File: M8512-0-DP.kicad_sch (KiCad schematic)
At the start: 0 parts

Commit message: Starting DP03
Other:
- added sheet DP03 (DP03.kicad_sch)
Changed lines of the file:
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@@
+    )
+  )
+  (sheet (at 36.195 102.235) (size 21.59 16.51) (fields_autoplaced)
+    (stroke (width 0.1524) (type solid) (color 0 0 0 0))
+    (fill (color 0 0 0 0.0000))
+    (property "Sheet name" "DP03" (id 0) (at 36.195 101.5234 0)
+      (effects (font (size 1.27 1.27)) (justify left bottom))
+    )
+    (property "Sheet file" "DP03.kicad_sch" (id 1) (at 36.195 119.3296 0)
+      (effects (font (size 1.27 1.27)) (justify left top))
     )
   )
@@
     (path "/0d0df2ac-f3f7-482e-ba7c-5f666b048a62" (page "2"))
     (path "/e53a1afb-1269-4ccc-9d39-72635457c7f7" (page "3"))
+    (path "/37ba04c2-b201-4f29-919c-bcd861d42582" (page "4"))
   )
   (symbol_instances
+    (path "/37ba04c2-b201-4f29-919c-bcd861d42582/3263b06a-f347-437b-94aa-a857004a7ea1"
+      (reference "E4") (unit 1) (value "MC10181") (footprint "")
+    )
+    (path "/37ba04c2-b201-4f29-919c-bcd861d42582/938d047d-ccaa-40b8-b822-1670ea770fee"
+      (reference "E7") (unit 1) (value "MC10109") (footprint "")
+    )
+    (path "/37ba04c2-b201-4f29-919c-bcd861d42582/d079f1e9-2d2b-44e5-ae40-de8d878751b0"
+      (reference "E7") (unit 2) (value "MC10109") (footprint "")
+    )
     (path "/0d0df2ac-f3f7-482e-ba7c-5f666b048a62/0f39e560-9336-4a48-a641-fec45e29a92d"
       (reference "E?") (unit 1) (value "MC10141") (footprint "")

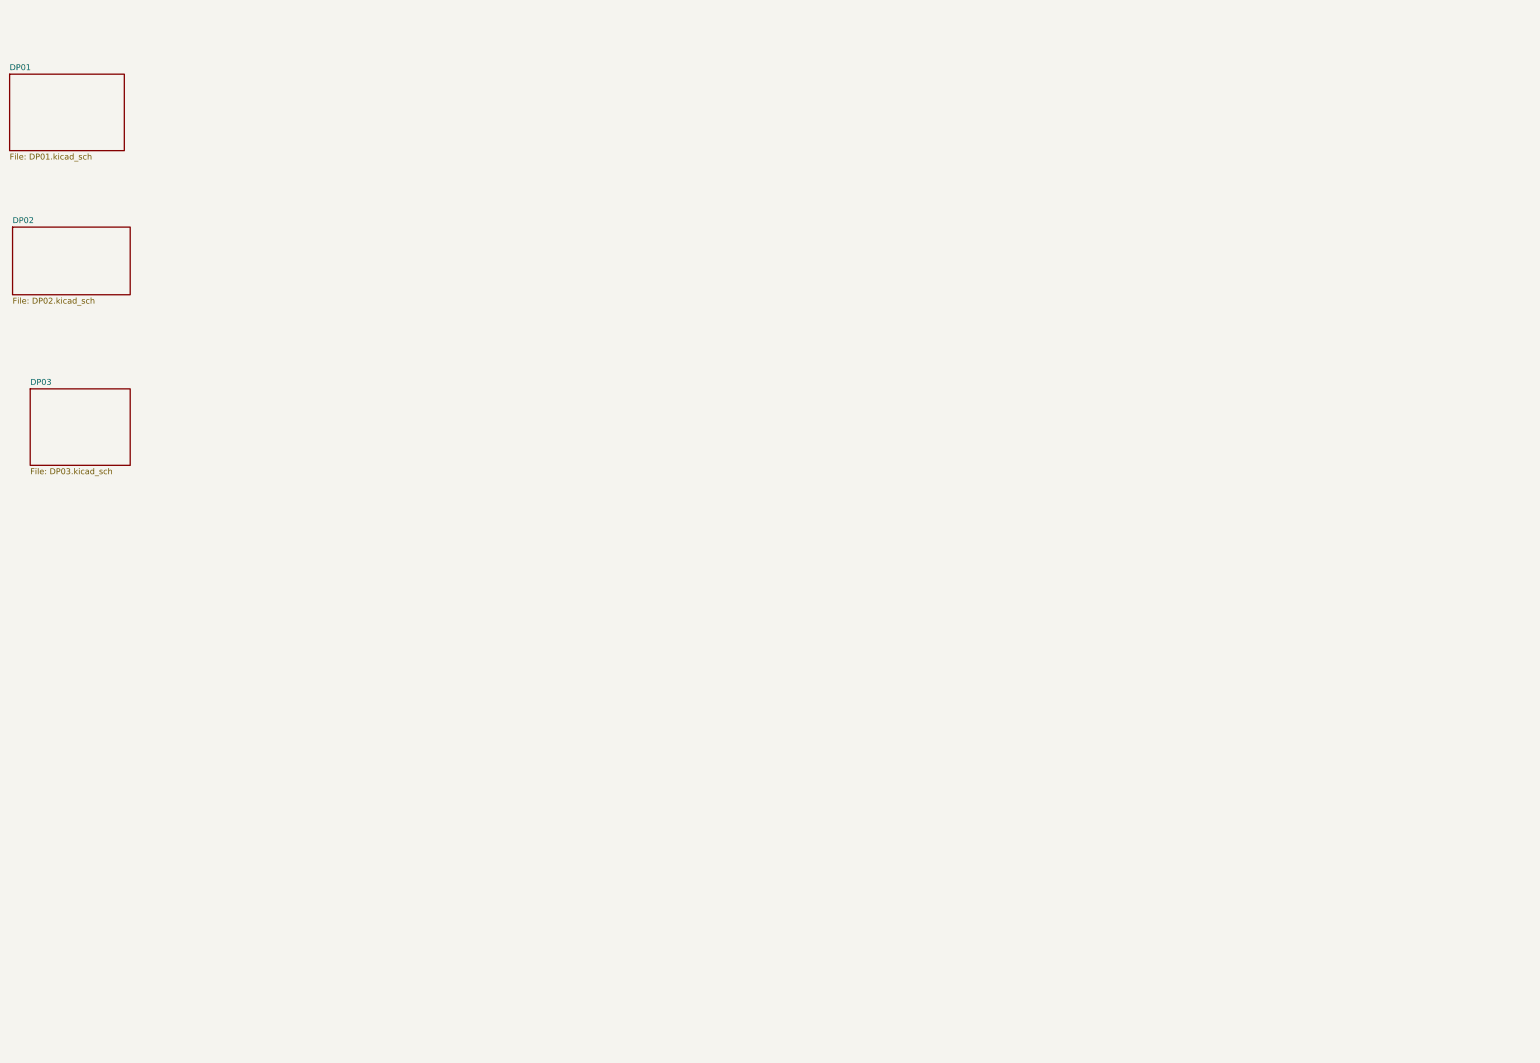
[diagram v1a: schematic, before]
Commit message: EDP is "done" but there is still much work to do to standardize and set up netlist export and verilog creation
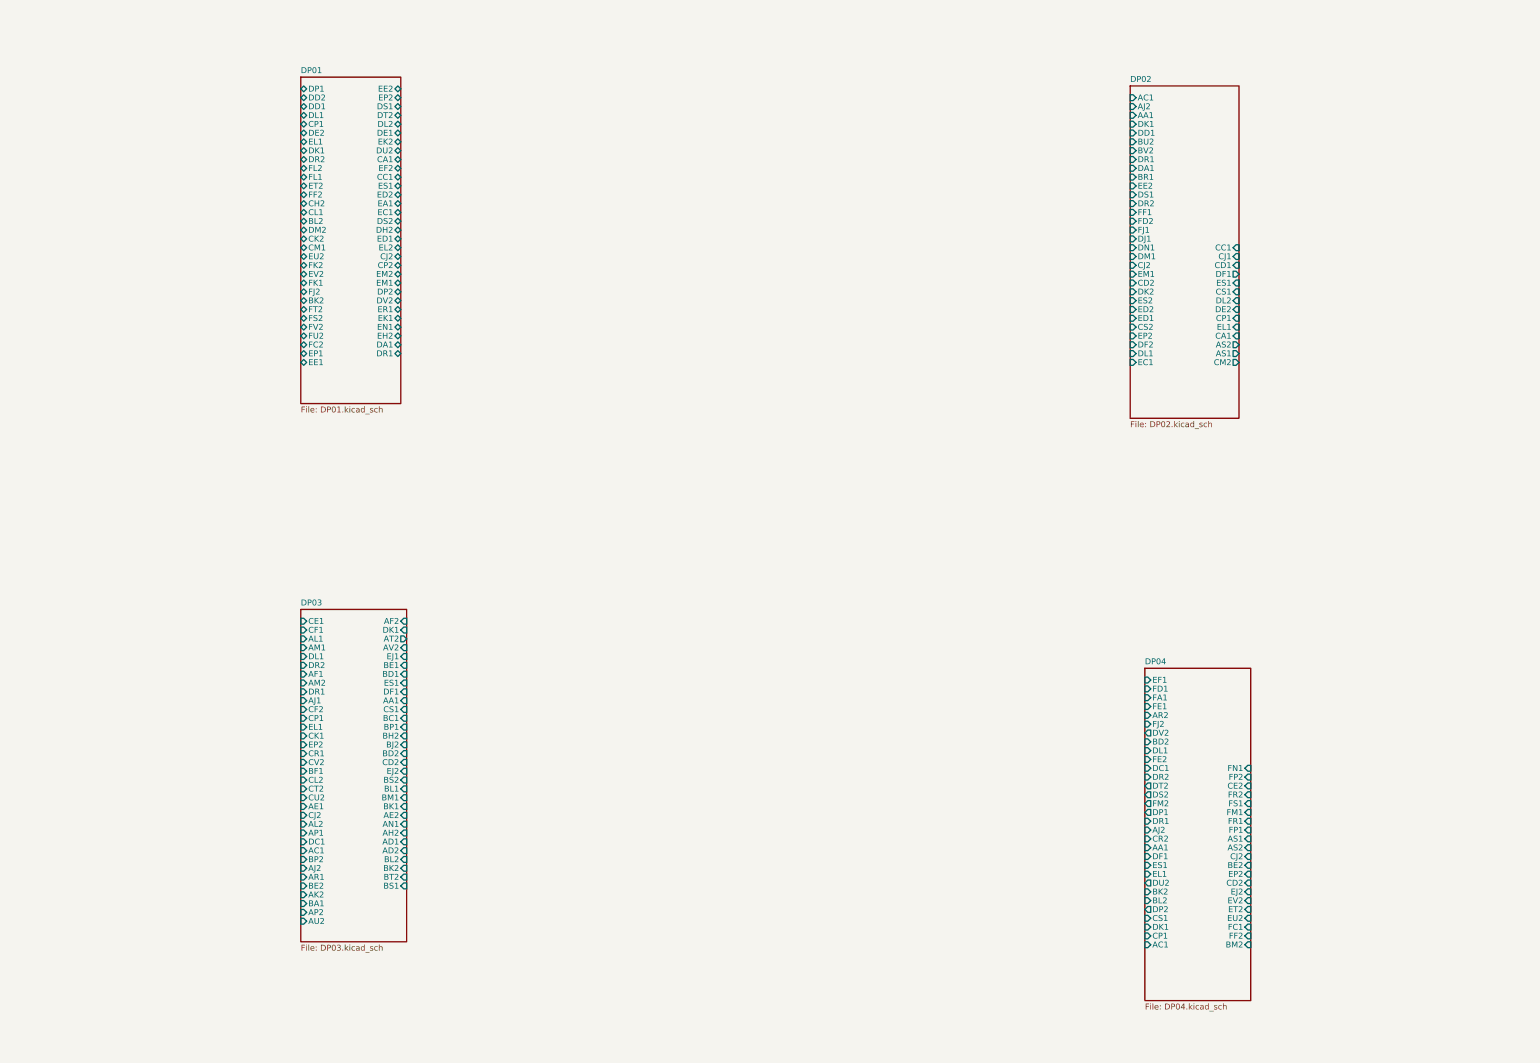
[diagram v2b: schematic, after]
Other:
- added sheet DP04 (DP04.kicad_sch)
- sheet DP01 ports: added BK2, BL2, CA1, CC1, CH2, CJ2, CK2, CL1, CM1, CP1, CP2, DA1, DD1, DD2, DE1, DE2, DH2, DK1, DL1, DL2, DM2, DP1, DP2, DR1, DR2, DS1, DS2, DT2, DU2, DV2, EA1, EC1, ED1, ED2, EE1, EE2, EF2, EH2, EK1, EK2, EL1, EL2, EM1, EM2, EN1, EP1, EP2, ER1, ES1, ET2, EU2, EV2, FC2, FF2, FJ2, FK1, FK2, FL1, FL2, FS2, FT2, FU2, FV2; removed none
- sheet DP02 ports: added AA1, AC1, AJ2, AS1, AS2, BR1, BU2, BV2, CA1, CC1, CD1, CD2, CJ1, CJ2, CM2, CP1, CS1, CS2, DA1, DD1, DE2, DF1, DF2, DJ1, DK1, DK2, DL1, DL2, DM1, DN1, DR1, DR2, DS1, EC1, ED1, ED2, EE2, EL1, EM1, EP2, ES1, ES2, FD2, FF1, FJ1; removed none
- sheet DP03 ports: added AA1, AC1, AD1, AD2, AE1, AE2, AF1, AF2, AH2, AJ1, AJ2, AK2, AL1, AL2, AM1, AM2, AN1, AP1, AP2, AR1, AT2, AU2, AV2, BA1, BC1, BD1, BD2, BE1, BE2, BF1, BH2, BJ2, BK1, BK2, BL1, BL2, BM1, BP1, BP2, BS1, BS2, BT2, CD2, CE1, CF1, CF2, CJ2, CK1, CL2, CP1, CR1, CS1, CT2, CU2, CV2, DC1, DF1, DK1, DL1, DR1, DR2, EJ1, EJ2, EL1, EP2, ES1; removed none
- title: DATA PATH AR REGISTER -> DATA PATH

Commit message: Adding backplane connector slowly and painfully
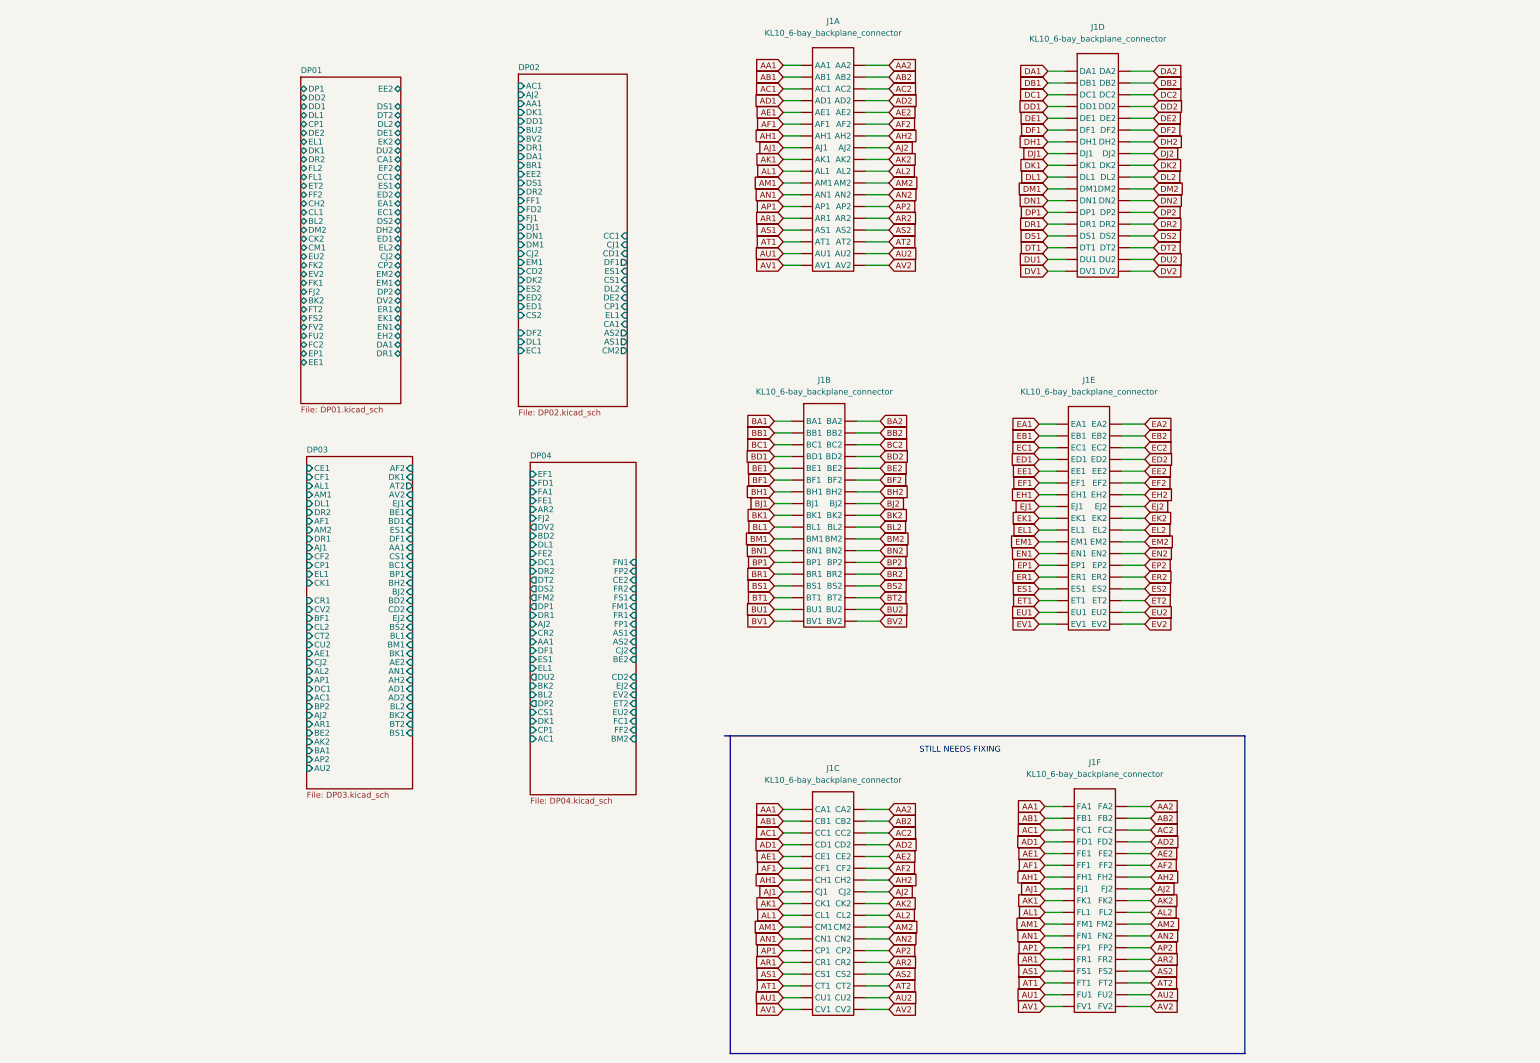
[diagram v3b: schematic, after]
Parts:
- added J1: KL10_6-bay_backplane_connector, symbol DEC20:KL10_6-bay_backplane_connector
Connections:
- new net AA1: J1.AA1, J1.CA1, J1.FA1
- new net AA2: J1.AA2, J1.CA2, J1.FA2
- new net AB1: J1.AB1, J1.CB1, J1.FB1
- new net AB2: J1.AB2, J1.CB2, J1.FB2
- new net AC1: J1.AC1, J1.CC1, J1.FC1
- new net AC2: J1.AC2, J1.CC2, J1.FC2
- new net AD1: J1.AD1, J1.CD1, J1.FD1
- new net AD2: J1.AD2, J1.CD2, J1.FD2
- new net AE1: J1.AE1, J1.CE1, J1.FE1
- new net AE2: J1.AE2, J1.CE2, J1.FE2
- new net AF1: J1.AF1, J1.CF1, J1.FF1
- new net AF2: J1.AF2, J1.CF2, J1.FF2
- new net AH1: J1.AH1, J1.CH1, J1.FH1
- new net AH2: J1.AH2, J1.CH2, J1.FH2
- new net AJ1: J1.AJ1, J1.CJ1, J1.FJ1
- new net AJ2: J1.AJ2, J1.CJ2, J1.FJ2
- new net AK1: J1.AK1, J1.CK1, J1.FK1
- new net AK2: J1.AK2, J1.CK2, J1.FK2
- new net AL1: J1.AL1, J1.CL1, J1.FL1
- new net AL2: J1.AL2, J1.CL2, J1.FL2
- new net AM1: J1.AM1, J1.CM1, J1.FM1
- new net AM2: J1.AM2, J1.CM2, J1.FM2
- new net AN1: J1.AN1, J1.CN1, J1.FN1
- new net AN2: J1.AN2, J1.CN2, J1.FN2
- new net AP1: J1.AP1, J1.CP1, J1.FP1
- new net AP2: J1.AP2, J1.CP2, J1.FP2
- new net AR1: J1.AR1, J1.CR1, J1.FR1
- new net AR2: J1.AR2, J1.CR2, J1.FR2
- new net AS1: J1.AS1, J1.CS1, J1.FS1
- new net AS2: J1.AS2, J1.CS2, J1.FS2
- new net AT1: J1.AT1, J1.CT1, J1.FT1
- new net AT2: J1.AT2, J1.CT2, J1.FT2
- new net AU1: J1.AU1, J1.CU1, J1.FU1
- new net AU2: J1.AU2, J1.CU2, J1.FU2
- new net AV1: J1.AV1, J1.CV1, J1.FV1
- new net AV2: J1.AV2, J1.CV2, J1.FV2
- new net BA1: J1.BA1
- new net BA2: J1.BA2
- new net BB1: J1.BB1
- new net BB2: J1.BB2
- new net BC1: J1.BC1
- new net BC2: J1.BC2
- new net BD1: J1.BD1
- new net BD2: J1.BD2
- new net BE1: J1.BE1
- new net BE2: J1.BE2
- new net BF1: J1.BF1
- new net BF2: J1.BF2
- new net BH1: J1.BH1
- new net BH2: J1.BH2
- new net BJ1: J1.BJ1
- new net BJ2: J1.BJ2
- new net BK1: J1.BK1
- new net BK2: J1.BK2
- new net BL1: J1.BL1
- new net BL2: J1.BL2
- new net BM1: J1.BM1
- new net BM2: J1.BM2
- new net BN1: J1.BN1
- new net BN2: J1.BN2
- new net BP1: J1.BP1
- new net BP2: J1.BP2
- new net BR1: J1.BR1
- new net BR2: J1.BR2
- new net BS1: J1.BS1
- new net BS2: J1.BS2
- new net BT1: J1.BT1
- new net BT2: J1.BT2
- new net BU1: J1.BU1
- new net BU2: J1.BU2
- new net BV1: J1.BV1
- new net BV2: J1.BV2
- new net DA1: J1.DA1
- new net DA2: J1.DA2
- new net DB1: J1.DB1
- new net DB2: J1.DB2
- new net DC1: J1.DC1
- new net DC2: J1.DC2
- new net DD1: J1.DD1
- new net DD2: J1.DD2
- new net DE1: J1.DE1
- new net DE2: J1.DE2
- new net DF1: J1.DF1
- new net DF2: J1.DF2
- new net DH1: J1.DH1
- new net DH2: J1.DH2
- new net DJ1: J1.DJ1
- new net DJ2: J1.DJ2
- new net DK1: J1.DK1
- new net DK2: J1.DK2
- new net DL1: J1.DL1
- new net DL2: J1.DL2
- new net DM1: J1.DM1
- new net DM2: J1.DM2
- new net DN1: J1.DN1
- new net DN2: J1.DN2
- new net DP1: J1.DP1
- new net DP2: J1.DP2
- new net DR1: J1.DR1
- new net DR2: J1.DR2
- new net DS1: J1.DS1
- new net DS2: J1.DS2
- new net DT1: J1.DT1
- new net DT2: J1.DT2
- new net DU1: J1.DU1
- new net DU2: J1.DU2
- new net DV1: J1.DV1
- new net DV2: J1.DV2
- new net EA1: J1.EA1
- new net EA2: J1.EA2
- new net EB1: J1.EB1
- new net EB2: J1.EB2
- new net EC1: J1.EC1
- new net EC2: J1.EC2
- new net ED1: J1.ED1
- new net ED2: J1.ED2
- new net EE1: J1.EE1
- new net EE2: J1.EE2
- new net EF1: J1.EF1
- new net EF2: J1.EF2
- new net EH1: J1.EH1
- new net EH2: J1.EH2
- new net EJ1: J1.EJ1
- new net EJ2: J1.EJ2
- new net EK1: J1.EK1
- new net EK2: J1.EK2
- new net EL1: J1.EL1
- new net EL2: J1.EL2
- new net EM1: J1.EM1
- new net EM2: J1.EM2
- new net EN1: J1.EN1
- new net EN2: J1.EN2
- new net EP1: J1.EP1
- new net EP2: J1.EP2
- new net ER1: J1.ER1
- new net ER2: J1.ER2
- new net ES1: J1.ES1
- new net ES2: J1.ES2
- new net ET1: J1.ET1
- new net ET2: J1.ET2
- new net EU1: J1.EU1
- new net EU2: J1.EU2
- new net EV1: J1.EV1
- new net EV2: J1.EV2
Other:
- sheet DP01 ports: added none; removed EP2
- sheet DP02 ports: added none; removed EP2
- sheet DP03 ports: added none; removed EP2
- sheet DP04 ports: added none; removed EP2
- note added: "STILL NEEDS FIXING"

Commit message: Convert all backplane refs to global labels and stick them on J1 pins. Convert all signal labels to global labels too so they are "global" inside M8512 board.
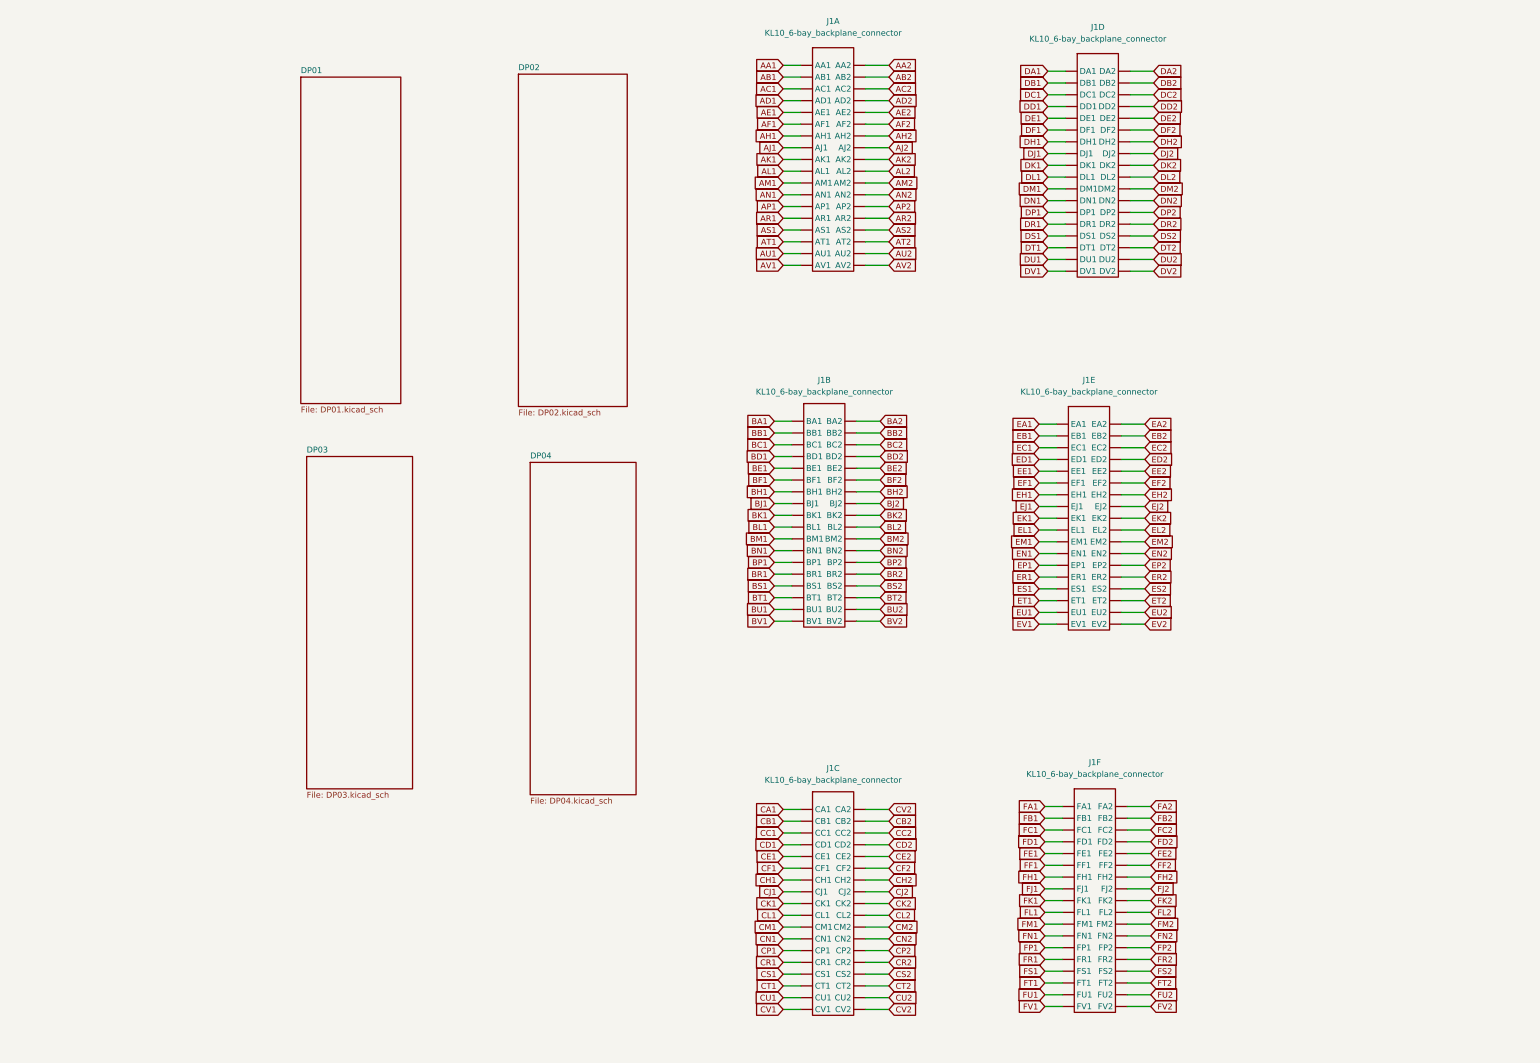
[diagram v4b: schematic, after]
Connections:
- net AA1: no longer J1.CA1, J1.FA1
- net AA2: no longer J1.CA2, J1.FA2
- net AB1: no longer J1.CB1, J1.FB1
- net AB2: no longer J1.CB2, J1.FB2
- net AC1: no longer J1.CC1, J1.FC1
- net AC2: no longer J1.CC2, J1.FC2
- net AD1: no longer J1.CD1, J1.FD1
- net AD2: no longer J1.CD2, J1.FD2
- net AE1: no longer J1.CE1, J1.FE1
- net AE2: no longer J1.CE2, J1.FE2
- net AF1: no longer J1.CF1, J1.FF1
- net AF2: no longer J1.CF2, J1.FF2
- net AH1: no longer J1.CH1, J1.FH1
- net AH2: no longer J1.CH2, J1.FH2
- net AJ1: no longer J1.CJ1, J1.FJ1
- net AJ2: no longer J1.CJ2, J1.FJ2
- net AK1: no longer J1.CK1, J1.FK1
- net AK2: no longer J1.CK2, J1.FK2
- net AL1: no longer J1.CL1, J1.FL1
- net AL2: no longer J1.CL2, J1.FL2
- net AM1: no longer J1.CM1, J1.FM1
- net AM2: no longer J1.CM2, J1.FM2
- net AN1: no longer J1.CN1, J1.FN1
- net AN2: no longer J1.CN2, J1.FN2
- net AP1: no longer J1.CP1, J1.FP1
- net AP2: no longer J1.CP2, J1.FP2
- net AR1: no longer J1.CR1, J1.FR1
- net AR2: no longer J1.CR2, J1.FR2
- net AS1: no longer J1.CS1, J1.FS1
- net AS2: no longer J1.CS2, J1.FS2
- net AT1: no longer J1.CT1, J1.FT1
- net AT2: no longer J1.CT2, J1.FT2
- net AU1: no longer J1.CU1, J1.FU1
- net AU2: no longer J1.CU2, J1.FU2
- net AV1: no longer J1.CV1, J1.FV1
- net AV2: no longer J1.CV2, J1.FV2
- new net CA1: J1.CA1
- new net CB1: J1.CB1
- new net CB2: J1.CB2
- new net CC1: J1.CC1
- new net CC2: J1.CC2
- new net CD1: J1.CD1
- new net CD2: J1.CD2
- new net CE1: J1.CE1
- new net CE2: J1.CE2
- new net CF1: J1.CF1
- new net CF2: J1.CF2
- new net CH1: J1.CH1
- new net CH2: J1.CH2
- new net CJ1: J1.CJ1
- new net CJ2: J1.CJ2
- new net CK1: J1.CK1
- new net CK2: J1.CK2
- new net CL1: J1.CL1
- new net CL2: J1.CL2
- new net CM1: J1.CM1
- new net CM2: J1.CM2
- new net CN1: J1.CN1
- new net CN2: J1.CN2
- new net CP1: J1.CP1
- new net CP2: J1.CP2
- new net CR1: J1.CR1
- new net CR2: J1.CR2
- new net CS1: J1.CS1
- new net CS2: J1.CS2
- new net CT1: J1.CT1
- new net CT2: J1.CT2
- new net CU1: J1.CU1
- new net CU2: J1.CU2
- new net CV1: J1.CV1
- new net CV2: J1.CA2, J1.CV2
- new net FA1: J1.FA1
- new net FA2: J1.FA2
- new net FB1: J1.FB1
- new net FB2: J1.FB2
- new net FC1: J1.FC1
- new net FC2: J1.FC2
- new net FD1: J1.FD1
- new net FD2: J1.FD2
- new net FE1: J1.FE1
- new net FE2: J1.FE2
- new net FF1: J1.FF1
- new net FF2: J1.FF2
- new net FH1: J1.FH1
- new net FH2: J1.FH2
- new net FJ1: J1.FJ1
- new net FJ2: J1.FJ2
- new net FK1: J1.FK1
- new net FK2: J1.FK2
- new net FL1: J1.FL1
- new net FL2: J1.FL2
- new net FM1: J1.FM1
- new net FM2: J1.FM2
- new net FN1: J1.FN1
- new net FN2: J1.FN2
- new net FP1: J1.FP1
- new net FP2: J1.FP2
- new net FR1: J1.FR1
- new net FR2: J1.FR2
- new net FS1: J1.FS1
- new net FS2: J1.FS2
- new net FT1: J1.FT1
- new net FT2: J1.FT2
- new net FU1: J1.FU1
- new net FU2: J1.FU2
- new net FV1: J1.FV1
- new net FV2: J1.FV2
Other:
- sheet DP01 ports: added none; removed BK2, BL2, CA1, CC1, CH2, CJ2, CK2, CL1, CM1, CP1, CP2, DA1, DD1, DD2, DE1, DE2, DH2, DK1, DL1, DL2, DM2, DP1, DP2, DR1, DR2, DS1, DS2, DT2, DU2, DV2, EA1, EC1, ED1, ED2, EE1, EE2, EF2, EH2, EK1, EK2, EL1, EL2, EM1, EM2, EN1, EP1, ER1, ES1, ET2, EU2, EV2, FC2, FF2, FJ2, FK1, FK2, FL1, FL2, FS2, FT2, FU2, FV2
- sheet DP02 ports: added none; removed AA1, AC1, AJ2, AS1, AS2, BR1, BU2, BV2, CA1, CC1, CD1, CD2, CJ1, CJ2, CM2, CP1, CS1, CS2, DA1, DD1, DE2, DF1, DF2, DJ1, DK1, DK2, DL1, DL2, DM1, DN1, DR1, DR2, DS1, EC1, ED1, ED2, EE2, EL1, EM1, ES1, ES2, FD2, FF1, FJ1
- sheet DP03 ports: added none; removed AA1, AC1, AD1, AD2, AE1, AE2, AF1, AF2, AH2, AJ1, AJ2, AK2, AL1, AL2, AM1, AM2, AN1, AP1, AP2, AR1, AT2, AU2, AV2, BA1, BC1, BD1, BD2, BE1, BE2, BF1, BH2, BJ2, BK1, BK2, BL1, BL2, BM1, BP1, BP2, BS1, BS2, BT2, CD2, CE1, CF1, CF2, CJ2, CK1, CL2, CP1, CR1, CS1, CT2, CU2, CV2, DC1, DF1, DK1, DL1, DR1, DR2, EJ1, EJ2, EL1, ES1
- sheet DP04 ports: added none; removed AA1, AC1, AJ2, AR2, AS1, AS2, BD2, BE2, BK2, BL2, BM2, CD2, CE2, CJ2, CP1, CR2, CS1, DC1, DF1, DK1, DL1, DP1, DP2, DR1, DR2, DS2, DT2, DU2, DV2, EF1, EJ2, EL1, ES1, ET2, EU2, EV2, FA1, FC1, FD1, FE1, FE2, FF2, FJ2, FM1, FM2, FN1, FP1, FP2, FR1, FR2, FS1
- note removed: "STILL NEEDS FIXING"
